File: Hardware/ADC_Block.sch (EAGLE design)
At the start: 28 parts, among them U1 ADS1015, U2 PCA9306

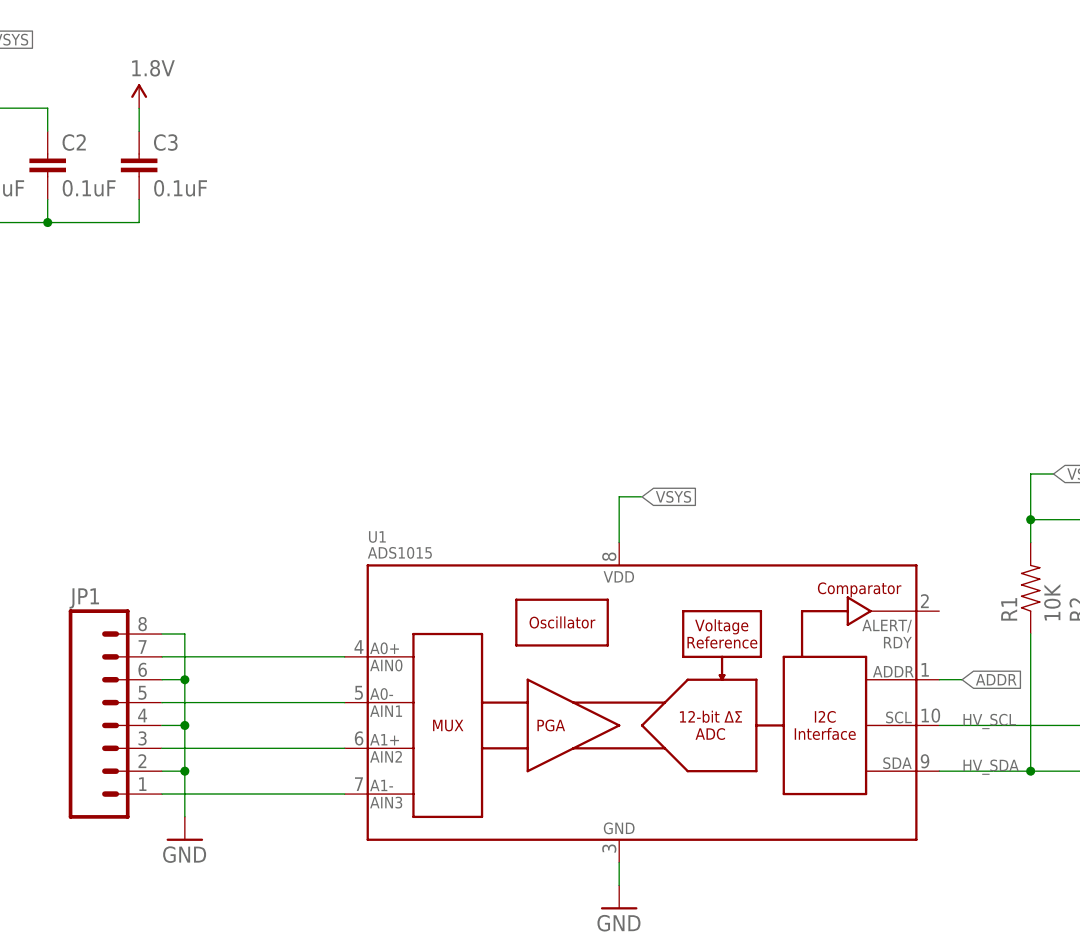
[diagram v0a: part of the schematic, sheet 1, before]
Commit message: made modifications to add a 3.3v reference voltage and power supply to measure potentiometers from. This will allow the block to be used in a stand alone mode.
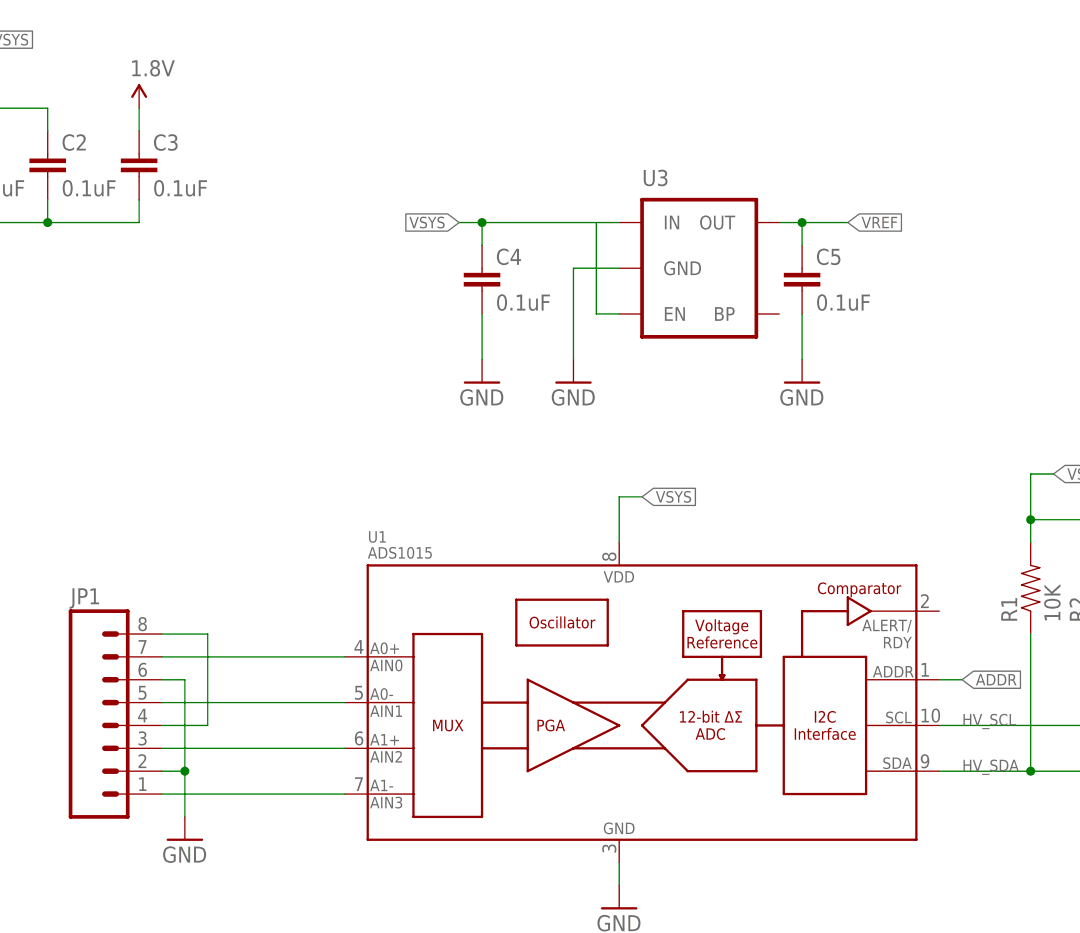
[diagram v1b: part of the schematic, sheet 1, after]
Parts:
- added C4, C5: 0.1uF, SparkFun-Capacitors:0.1UF-25V(+80/-20%)(0603)
- added U3: (no value), SparkFun-PowerIC:MIC52053.3V
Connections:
- new net VREF: C5.1, JP1.4, JP1.8, U3.OUT
- net GND: now also C4.2, C5.2, U3.GND; no longer JP1.4, JP1.8
- net VSYS: now also C4.1, U3.EN, U3.IN
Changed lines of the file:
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@@
 <?xml version="1.0" encoding="utf-8"?>
 <!DOCTYPE eagle SYSTEM "eagle.dtd">
-<eagle version="6.6.0">
+<eagle version="6.5.0">
 <drawing>
 <settings>
@@
 <part name="FID3" library="SparkFun-Aesthetics" deviceset="FIDUCIAL" device="1X2" value="FIDUCIAL1X2"/>
 <part name="FID4" library="SparkFun-Aesthetics" deviceset="FIDUCIAL" device="1X2" value="FIDUCIAL1X2"/>
+<part name="U3" library="SparkFun-PowerIC" deviceset="MIC5205" device="3.3V"/>
+<part name="C4" library="SparkFun-Capacitors" deviceset="0.1UF-25V(+80/-20%)(0603)" device="" value="0.1uF"/>
+<part name="C5" library="SparkFun-Capacitors" deviceset="0.1UF-25V(+80/-20%)(0603)" device="" value="0.1uF"/>
+<part name="GND8" library="SparkFun-Aesthetics" deviceset="GND" device=""/>
+<part name="GND9" library="SparkFun-Aesthetics" deviceset="GND" device=""/>
+<part name="GND10" library="SparkFun-Aesthetics" deviceset="GND" device=""/>
 </parts>
 <sheets>
@@
 <instance part="FID3" gate="G$1" x="238.76" y="33.02"/>
 <instance part="FID4" gate="G$1" x="243.84" y="33.02"/>
+<instance part="U3" gate="G$1" x="104.14" y="144.78"/>
+<instance part="C4" gate="G$1" x="78.74" y="142.24"/>
+<instance part="C5" gate="G$1" x="114.3" y="142.24"/>
+<instance part="GND8" gate="1" x="78.74" y="132.08"/>
+<instance part="GND9" gate="1" x="88.9" y="132.08"/>
+<instance part="GND10" gate="1" x="114.3" y="132.08"/>
 </instances>
 <busses>
@@
 </segment>
 <segment>
-<pinref part="JP1" gate="G$1" pin="8"/>
-<wire x1="43.18" y1="104.14" x2="45.72" y2="104.14" width="0.1524" layer="91"/>
-<wire x1="45.72" y1="104.14" x2="45.72" y2="99.06" width="0.1524" layer="91"/>
 <pinref part="JP1" gate="G$1" pin="2"/>
-<wire x1="45.72" y1="99.06" x2="45.72" y2="93.98" width="0.1524" layer="91"/>
-<wire x1="45.72" y1="93.98" x2="45.72" y2="88.9" width="0.1524" layer="91"/>
+<wire x1="45.72" y1="99.06" x2="45.72" y2="88.9" width="0.1524" layer="91"/>
 <wire x1="45.72" y1="88.9" x2="43.18" y2="88.9" width="0.1524" layer="91"/>
-<pinref part="JP1" gate="G$1" pin="4"/>
-<wire x1="43.18" y1="93.98" x2="45.72" y2="93.98" width="0.1524" layer="91"/>
-<junction x="45.72" y="93.98"/>
 <pinref part="JP1" gate="G$1" pin="6"/>
 <wire x1="43.18" y1="99.06" x2="45.72" y2="99.06" width="0.1524" layer="91"/>
-<junction x="45.72" y="99.06"/>
 <pinref part="GND7" gate="1" pin="GND"/>
 <wire x1="45.72" y1="83.82" x2="45.72" y2="88.9" width="0.1524" layer="91"/>
 <junction x="45.72" y="88.9"/>
+</segment>
+<segment>
+<pinref part="C4" gate="G$1" pin="2"/>
+<pinref part="GND8" gate="1" pin="GND"/>
+<wire x1="78.74" y1="134.62" x2="78.74" y2="139.7" width="0.1524" layer="91"/>
+</segment>
+<segment>
+<pinref part="U3" gate="G$1" pin="GND"/>
+<pinref part="GND9" gate="1" pin="GND"/>
+<wire x1="93.98" y1="144.78" x2="88.9" y2="144.78" width="0.1524" layer="91"/>
+<wire x1="88.9" y1="144.78" x2="88.9" y2="134.62" width="0.1524" layer="91"/>
+</segment>
+<segment>
+<pinref part="C5" gate="G$1" pin="2"/>
+<pinref part="GND10" gate="1" pin="GND"/>
+<wire x1="114.3" y1="134.62" x2="114.3" y2="139.7" width="0.1524" layer="91"/>
 </segment>
 </net>
@@
 <wire x1="35.56" y1="33.02" x2="30.48" y2="33.02" width="0.1524" layer="91"/>
 </segment>
+<segment>
+<pinref part="U3" gate="G$1" pin="EN"/>
+<wire x1="93.98" y1="139.7" x2="91.44" y2="139.7" width="0.1524" layer="91"/>
+<wire x1="91.44" y1="139.7" x2="91.44" y2="149.86" width="0.1524" layer="91"/>
+<pinref part="U3" gate="G$1" pin="IN"/>
+<wire x1="91.44" y1="149.86" x2="93.98" y2="149.86" width="0.1524" layer="91"/>
+<wire x1="91.44" y1="149.86" x2="78.74" y2="149.86" width="0.1524" layer="91"/>
+<wire x1="78.74" y1="149.86" x2="78.74" y2="147.32" width="0.1524" layer="91"/>
+<pinref part="C4" gate="G$1" pin="1"/>
+<wire x1="78.74" y1="149.86" x2="76.2" y2="149.86" width="0.1524" layer="91"/>
+<junction x="78.74" y="149.86"/>
+<label x="76.2" y="149.86" size="1.27" layer="95" rot="R180" xref="yes"/>
+</segment>
 </net>
 <net name="N$3" class="0">
@@
 </segment>
 </net>
+<net name="VREF" class="0">
+<segment>
+<pinref part="JP1" gate="G$1" pin="4"/>
+<wire x1="43.18" y1="93.98" x2="48.26" y2="93.98" width="0.1524" layer="91"/>
+<wire x1="48.26" y1="93.98" x2="48.26" y2="104.14" width="0.1524" layer="91"/>
+<pinref part="JP1" gate="G$1" pin="8"/>
+<wire x1="43.18" y1="104.14" x2="48.26" y2="104.14" width="0.1524" layer="91"/>
+</segment>
+<segment>
+<pinref part="U3" gate="G$1" pin="OUT"/>
+<pinref part="C5" gate="G$1" pin="1"/>
+<wire x1="111.76" y1="149.86" x2="114.3" y2="149.86" width="0.1524" layer="91"/>
+<wire x1="114.3" y1="149.86" x2="114.3" y2="147.32" width="0.1524" layer="91"/>
+<wire x1="114.3" y1="149.86" x2="119.38" y2="149.86" width="0.1524" layer="91"/>
+<junction x="114.3" y="149.86"/>
+<label x="119.38" y="149.86" size="1.27" layer="95" xref="yes"/>
+</segment>
+</net>

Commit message: updated rev number
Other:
- note added: "v20"
- note removed: "v10"
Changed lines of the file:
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@@
 1001010 (0x4A)
 1001011 (0x4B)</text>
-<text x="237.744" y="6.604" size="2.54" layer="94">v10</text>
+<text x="237.744" y="6.604" size="2.54" layer="94">v20</text>
 <text x="165.1" y="7.62" size="3.81" layer="94">M Hord</text>
 </plain>

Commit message: corrected issues in github
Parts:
- removed U$2: EDISON_CONNECTOR_FULLMOUNTING_HOLES, Edison:EDISON_CONNECTOR_FULLMOUNTING_HOLES
- removed U$3: EDISON_CONNECTOR_FULLHEADER, Edison:EDISON_CONNECTOR_FULLHEADER
- added JP2: EDISON_CONNECTOR_FULLMOUNTING_HOLES, SparkFun-Boards:EDISON_CONNECTOR_FULLMOUNTING_HOLES
- added JP3: EDISON_CONNECTOR_FULLHEADER, SparkFun-Boards:EDISON_CONNECTOR_FULLHEADER
- FRAME1, FRAME2: value FRAME-LETTER -> (none)
- JP1: device SparkFun-Connectors:M081X08 -> SparkFun-Connectors:M08
- U3: value (none) -> 3.3V
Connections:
- net 1.8V: now also JP2.1.8V, JP3.1.8V; no longer U$2.1.8V, U$3.1.8V
- net 3.3V: now also JP2.3.3V@1, JP2.3.3V@2, JP3.3.3V@1, JP3.3.3V@2; no longer U$2.3.3V@1, U$2.3.3V@2, U$3.3.3V@1, U$3.3.3V@2
- net DCIN: now also JP2.DCIN, JP3.DCIN; no longer U$2.DCIN, U$3.DCIN
- net FAULT: now also JP2.FAULT, JP3.FAULT; no longer U$2.FAULT, U$3.FAULT
- net FW_RCVR: now also JP2.FW_RCVR, JP3.FW_RCVR; no longer U$2.FW_RCVR, U$3.FW_RCVR
- net GND: now also JP2.GND@1, JP2.GND@2, JP2.GND@3, JP2.GND@4, JP2.GND@5, JP2.GND@6, JP3.GND@1, JP3.GND@2, JP3.GND@3, JP3.GND@4, JP3.GND@5, JP3.GND@6; no longer U$2.GND@1, U$2.GND@2, U$2.GND@3, U$2.GND@4, U$2.GND@5, U$2.GND@6, U$3.GND@1, U$3.GND@2, U$3.GND@3, U$3.GND@4, U$3.GND@5, U$3.GND@6
- net GP109_SPI_2_CLK: now also JP2.GP109_SPI_2_CLK, JP3.GP109_SPI_2_CLK; no longer U$2.GP109_SPI_2_CLK, U$3.GP109_SPI_2_CLK
- net GP110_SPI_2_FS0: now also JP2.GP110_SPI_2_FS0, JP3.GP110_SPI_2_FS0; no longer U$2.GP110_SPI_2_FS0, U$3.GP110_SPI_2_FS0
- net GP111_SPI_2_FS1: now also JP2.GP111_SPI_2_FS1, JP3.GP111_SPI_2_FS1; no longer U$2.GP111_SPI_2_FS1, U$3.GP111_SPI_2_FS1
- net GP114_SPI_2_RXD: now also JP2.GP114_SPI_2_RXD, JP3.GP114_SPI_2_RXD; no longer U$2.GP114_SPI_2_RXD, U$3.GP114_SPI_2_RXD
- net GP115_SPI_2_TXD: now also JP2.GP115_SPI_2_TXD, JP3.GP115_SPI_2_TXD; no longer U$2.GP115_SPI_2_TXD, U$3.GP115_SPI_2_TXD
- net GP128_UART_1_CTS: now also JP2.GP128_UART_1_CTS, JP3.GP128_UART_1_CTS; no longer U$2.GP128_UART_1_CTS, U$3.GP128_UART_1_CTS
- net GP129_UART_1_RTS: now also JP2.GP129_UART_1_RTS, JP3.GP129_UART_1_RTS; no longer U$2.GP129_UART_1_RTS, U$3.GP129_UART_1_RTS
- net GP12_PWM0: now also JP2.GP12_PWM0, JP3.GP12_PWM0; no longer U$2.GP12_PWM0, U$3.GP12_PWM0
- net GP130_UART_1_RX: now also JP2.GP130_UART_1_RX, JP3.GP130_UART_1_RX; no longer U$2.GP130_UART_1_RX, U$3.GP130_UART_1_RX
- net GP131_UART_1_TX: now also JP2.GP131_UART_1_TX, JP3.GP131_UART_1_TX; no longer U$2.GP131_UART_1_TX, U$3.GP131_UART_1_TX
- net GP134_UART_2_RX: now also JP2.GP134_UART_2_RX, JP3.GP134_UART_2_RX; no longer U$2.GP134_UART_2_RX, U$3.GP134_UART_2_RX
- net GP135_UART_2_TX: now also JP2.GP135_UART_2_TX, JP3.GP135_UART_2_TX; no longer U$2.GP135_UART_2_TX, U$3.GP135_UART_2_TX
- net GP13_PWM1: now also JP2.GP13_PWM1, JP3.GP13_PWM1; no longer U$2.GP13_PWM1, U$3.GP13_PWM1
- net GP14: now also JP2.GP14, JP3.GP14; no longer U$2.GP14, U$3.GP14
- net GP15: now also JP2.GP15, JP3.GP15; no longer U$2.GP15, U$3.GP15
- net GP165: now also JP2.GP165, JP3.GP165; no longer U$2.GP165, U$3.GP165
- net GP182_PWM2: now also JP2.GP182_PWM2, JP3.GP182_PWM2; no longer U$2.GP182_PWM2, U$3.GP182_PWM2
- net GP183_PWM3: now also JP2.GP183_PWM3, JP3.GP183_PWM3; no longer U$2.GP183_PWM3, U$3.GP183_PWM3
- net GP19_I2C_1_SCL: now also JP2.GP19_I2C_1_SCL, JP3.GP19_I2C_1_SCL; no longer U$2.GP19_I2C_1_SCL, U$3.GP19_I2C_1_SCL
- net GP20_I2C_1_SDA: now also JP2.GP20_I2C_1_SDA, JP3.GP20_I2C_1_SDA; no longer U$2.GP20_I2C_1_SDA, U$3.GP20_I2C_1_SDA
- net GP27_I2C_6_SCL: now also JP2.GP27_I2C_6_SCL, JP3.GP27_I2C_6_SCL; no longer U$2.GP27_I2C_6_SCL, U$3.GP27_I2C_6_SCL
- net GP28_I2C_6_SDA: now also JP2.GP28_I2C_6_SDA, JP3.GP28_I2C_6_SDA; no longer U$2.GP28_I2C_6_SDA, U$3.GP28_I2C_6_SDA
- net GP40_I2S_2_CLK: now also JP2.GP40_I2S_2_CLK, JP3.GP40_I2S_2_CLK; no longer U$2.GP40_I2S_2_CLK, U$3.GP40_I2S_2_CLK
- net GP41_I2S_2_FS: now also JP2.GP41_I2S_2_FS, JP3.GP41_I2S_2_FS; no longer U$2.GP41_I2S_2_FS, U$3.GP41_I2S_2_FS
- net GP42_I2S_2_RXD: now also JP2.GP42_I2S_2_RXD, JP3.GP42_I2S_2_RXD; no longer U$2.GP42_I2S_2_RXD, U$3.GP42_I2S_2_RXD
- net GP43_I2S_2_TXD: now also JP2.GP43_I2S_2_TXD, JP3.GP43_I2S_2_TXD; no longer U$2.GP43_I2S_2_TXD, U$3.GP43_I2S_2_TXD
- net GP44: now also JP2.GP44, JP3.GP44; no longer U$2.GP44, U$3.GP44
- net GP45: now also JP2.GP45, JP3.GP45; no longer U$2.GP45, U$3.GP45
- net GP46: now also JP2.GP46, JP3.GP46; no longer U$2.GP46, U$3.GP46
- net GP47: now also JP2.GP47, JP3.GP47; no longer U$2.GP47, U$3.GP47
- net GP48: now also JP2.GP48, JP3.GP48; no longer U$2.GP48, U$3.GP48
- net GP49: now also JP2.GP49, JP3.GP49; no longer U$2.GP49, U$3.GP49
- net GP77_SD_0_CD#: now also JP2.GP77_SD_0_CD#, JP3.GP77_SD_0_CD#; no longer U$2.GP77_SD_0_CD#, U$3.GP77_SD_0_CD#
- net GP78_SD_0_CLK: now also JP2.GP78_SD_0_CLK, JP3.GP78_SD_0_CLK; no longer U$2.GP78_SD_0_CLK, U$3.GP78_SD_0_CLK
- net GP79_SD_0_CMD: now also JP2.GP79_SD_0_CMD, JP3.GP79_SD_0_CMD; no longer U$2.GP79_SD_0_CMD, U$3.GP79_SD_0_CMD
- net GP80_SD_0_DAT0: now also JP2.GP80_SD_0_DAT0, JP3.GP80_SD_0_DAT0; no longer U$2.GP80_SD_0_DAT0, U$3.GP80_SD_0_DAT0
- net GP81_SD_0_DAT1: now also JP2.GP81_SD_0_DAT1, JP3.GP81_SD_0_DAT1; no longer U$2.GP81_SD_0_DAT1, U$3.GP81_SD_0_DAT1
- net GP82_SD_0_DAT2: now also JP2.GP82_SD_0_DAT2, JP3.GP82_SD_0_DAT2; no longer U$2.GP82_SD_0_DAT2, U$3.GP82_SD_0_DAT2
- net GP83_SD_0_DAT3: now also JP2.GP83_SD_0_DAT3, JP3.GP83_SD_0_DAT3; no longer U$2.GP83_SD_0_DAT3, U$3.GP83_SD_0_DAT3
- net GP84_SD_CLK_FB: now also JP2.GP84_SD_CLK_FB, JP3.GP84_SD_CLK_FB; no longer U$2.GP84_SD_CLK_FB, U$3.GP84_SD_CLK_FB
- net MSIC_SLP_CLK: now also JP2.MSIC_SLP_CLK, JP3.MSIC_SLP_CLK; no longer U$2.MSIC_SLP_CLK, U$3.MSIC_SLP_CLK
- net OSC_CLK_OUT: now also JP2.OSC_CLK_OUT_0, JP3.OSC_CLK_OUT_0; no longer U$2.OSC_CLK_OUT_0, U$3.OSC_CLK_OUT_0
- net PSW: now also JP2.PSW, JP3.PSW; no longer U$2.PSW, U$3.PSW
- net PWRBTN#: now also JP2.PWRBTN#, JP3.PWRBTN#; no longer U$2.PWRBTN#, U$3.PWRBTN#
- net RCVR_MODE: now also JP2.RCVR_MODE, JP3.RCVR_MODE; no longer U$2.RCVR_MODE, U$3.RCVR_MODE
- net RESET_OUT#: now also JP2.RESET_OUT#, JP3.RESET_OUT#; no longer U$2.RESET_OUT#, U$3.RESET_OUT#
- net USB_DN: now also JP2.USB_DN, JP3.USB_DN; no longer U$2.USB_DN, U$3.USB_DN
- net USB_DP: now also JP2.USB_DP, JP3.USB_DP; no longer U$2.USB_DP, U$3.USB_DP
- net USB_ID: now also JP2.USB_ID, JP3.USB_ID; no longer U$2.USB_ID, U$3.USB_ID
- net USB_VBUS: now also JP2.USB_VBUS, JP3.USB_VBUS; no longer U$2.USB_VBUS, U$3.USB_VBUS
- net VSYS: now also JP2.VSYS@1, JP2.VSYS@2, JP2.VSYS@3, JP3.VSYS@1, JP3.VSYS@2, JP3.VSYS@3; no longer U$2.VSYS@1, U$2.VSYS@2, U$2.VSYS@3, U$3.VSYS@1, U$3.VSYS@2, U$3.VSYS@3
- net V_BAT_BKUP: now also JP2.V_VAT_BKUP, JP3.V_VAT_BKUP; no longer U$2.V_VAT_BKUP, U$3.V_VAT_BKUP
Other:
- note added: "Revised 3/15 - Casey (adding Vref 3.3V, IC still uses internal VREF)"

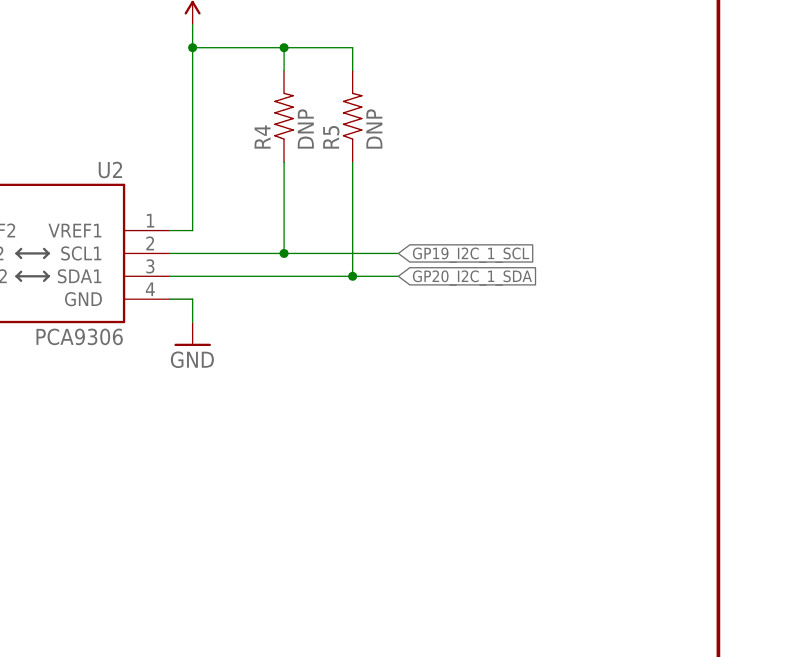
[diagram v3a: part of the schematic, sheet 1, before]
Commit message: added Bus selection to board
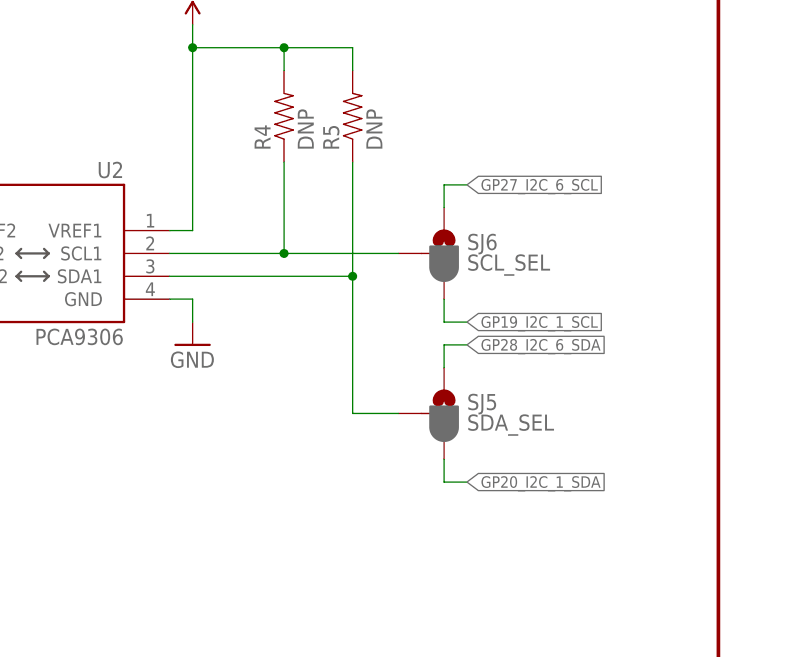
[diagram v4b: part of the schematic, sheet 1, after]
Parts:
- added SJ5: SDA_SEL, SparkFun-Passives:JUMPER-PAD-3-2OF3_NC_BY_PASTE
- added SJ6: SCL_SEL, SparkFun-Passives:JUMPER-PAD-3-2OF3_NC_BY_PASTE
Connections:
- new net N$2: R4.1, SJ6.2, U2.SCL1
- new net N$4: R5.1, SJ5.2, U2.SDA1
- net GP19_I2C_1_SCL: now also SJ6.3; no longer R4.1, U2.SCL1
- net GP20_I2C_1_SDA: now also SJ5.3; no longer R5.1, U2.SDA1
- net GP27_I2C_6_SCL: now also SJ6.1
- net GP28_I2C_6_SDA: now also SJ5.1
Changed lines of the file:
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@@
 <part name="GND9" library="SparkFun-Aesthetics" deviceset="GND" device=""/>
 <part name="GND10" library="SparkFun-Aesthetics" deviceset="GND" device=""/>
+<part name="SJ5" library="SparkFun-Passives" deviceset="JUMPER-PAD-3-2OF3_NC_BY_PASTE" device="" value="SDA_SEL"/>
+<part name="SJ6" library="SparkFun-Passives" deviceset="JUMPER-PAD-3-2OF3_NC_BY_PASTE" device="" value="SCL_SEL"/>
 </parts>
 <sheets>
@@
 <instance part="GND9" gate="1" x="88.9" y="132.08"/>
 <instance part="GND10" gate="1" x="114.3" y="132.08"/>
+<instance part="SJ5" gate="G$1" x="218.44" y="76.2"/>
+<instance part="SJ6" gate="G$1" x="218.44" y="93.98"/>
 </instances>
 <busses>
@@
 </segment>
 </net>
-<net name="GP19_I2C_1_SCL" class="0">
-<segment>
-<pinref part="U2" gate="G$1" pin="SCL1"/>
-<pinref part="R4" gate="G$1" pin="1"/>
-<wire x1="187.96" y1="93.98" x2="200.66" y2="93.98" width="0.1524" layer="91"/>
-<wire x1="200.66" y1="93.98" x2="200.66" y2="104.14" width="0.1524" layer="91"/>
-<wire x1="200.66" y1="93.98" x2="213.36" y2="93.98" width="0.1524" layer="91"/>
-<junction x="200.66" y="93.98"/>
-<label x="213.36" y="93.98" size="1.27" layer="95" xref="yes"/>
-</segment>
-</net>
 <net name="GP20_I2C_1_SDA" class="0">
 <segment>
-<pinref part="U2" gate="G$1" pin="SDA1"/>
-<pinref part="R5" gate="G$1" pin="1"/>
-<wire x1="187.96" y1="91.44" x2="208.28" y2="91.44" width="0.1524" layer="91"/>
-<wire x1="208.28" y1="91.44" x2="208.28" y2="104.14" width="0.1524" layer="91"/>
-<wire x1="208.28" y1="91.44" x2="213.36" y2="91.44" width="0.1524" layer="91"/>
-<junction x="208.28" y="91.44"/>
-<label x="213.36" y="91.44" size="1.27" layer="95" xref="yes"/>
+<pinref part="SJ5" gate="G$1" pin="3"/>
+<wire x1="218.44" y1="71.12" x2="218.44" y2="68.58" width="0.1524" layer="91"/>
+<wire x1="218.44" y1="68.58" x2="220.98" y2="68.58" width="0.1524" layer="91"/>
+<label x="220.98" y="68.58" size="1.27" layer="95" xref="yes"/>
 </segment>
 </net>
@@
 </segment>
 </net>
+<net name="N$2" class="0">
+<segment>
+<pinref part="U2" gate="G$1" pin="SCL1"/>
+<pinref part="SJ6" gate="G$1" pin="2"/>
+<wire x1="187.96" y1="93.98" x2="200.66" y2="93.98" width="0.1524" layer="91"/>
+<pinref part="R4" gate="G$1" pin="1"/>
+<wire x1="200.66" y1="93.98" x2="213.36" y2="93.98" width="0.1524" layer="91"/>
+<wire x1="200.66" y1="104.14" x2="200.66" y2="93.98" width="0.1524" layer="91"/>
+<junction x="200.66" y="93.98"/>
+</segment>
+</net>
+<net name="N$4" class="0">
+<segment>
+<pinref part="R5" gate="G$1" pin="1"/>
+<wire x1="208.28" y1="104.14" x2="208.28" y2="91.44" width="0.1524" layer="91"/>
+<pinref part="U2" gate="G$1" pin="SDA1"/>
+<wire x1="208.28" y1="91.44" x2="187.96" y2="91.44" width="0.1524" layer="91"/>
+<pinref part="SJ5" gate="G$1" pin="2"/>
+<wire x1="208.28" y1="91.44" x2="208.28" y2="76.2" width="0.1524" layer="91"/>
+<wire x1="208.28" y1="76.2" x2="213.36" y2="76.2" width="0.1524" layer="91"/>
+<junction x="208.28" y="91.44"/>
+</segment>
+</net>
+<net name="GP28_I2C_6_SDA" class="0">
+<segment>
+<pinref part="SJ5" gate="G$1" pin="1"/>
+<wire x1="218.44" y1="81.28" x2="218.44" y2="83.82" width="0.1524" layer="91"/>
+<wire x1="218.44" y1="83.82" x2="220.98" y2="83.82" width="0.1524" layer="91"/>
+<label x="220.98" y="83.82" size="1.27" layer="95" xref="yes"/>
+</segment>
+</net>
+<net name="GP19_I2C_1_SCL" class="0">
+<segment>
+<pinref part="SJ6" gate="G$1" pin="3"/>
+<wire x1="218.44" y1="88.9" x2="218.44" y2="86.36" width="0.1524" layer="91"/>
+<wire x1="218.44" y1="86.36" x2="220.98" y2="86.36" width="0.1524" layer="91"/>
+<label x="220.98" y="86.36" size="1.27" layer="95" xref="yes"/>
+</segment>
+</net>
+<net name="GP27_I2C_6_SCL" class="0">
+<segment>
+<pinref part="SJ6" gate="G$1" pin="1"/>
+<wire x1="218.44" y1="99.06" x2="218.44" y2="101.6" width="0.1524" layer="91"/>
+<wire x1="218.44" y1="101.6" x2="220.98" y2="101.6" width="0.1524" layer="91"/>
+<label x="220.98" y="101.6" size="1.27" layer="95" xref="yes"/>
+</segment>
+</net>

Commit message: added note to SCH
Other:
- note added: "Note: Bus Selection Default to I2C-1"
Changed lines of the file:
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@@
 <text x="165.1" y="7.62" size="3.81" layer="94">M Hord</text>
 <text x="172.72" y="38.1" size="1.778" layer="94">Revised 3/15 - Casey (adding Vref 3.3V, IC still uses internal VREF)</text>
+<text x="215.9" y="73.66" size="1.27" layer="91" rot="R180">Note: Bus Selection
+Default to I2C-1</text>
 </plain>
 <instances>
